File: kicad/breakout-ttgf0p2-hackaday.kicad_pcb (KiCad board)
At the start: 2 copper layers, 55 x 85 mm, 7 parts, among them J1 Conn_01x17, J2 Conn_01x20, J3 Conn_01x17, J4 Conn_01x20, U1 TT_GF_0p2_ASIC

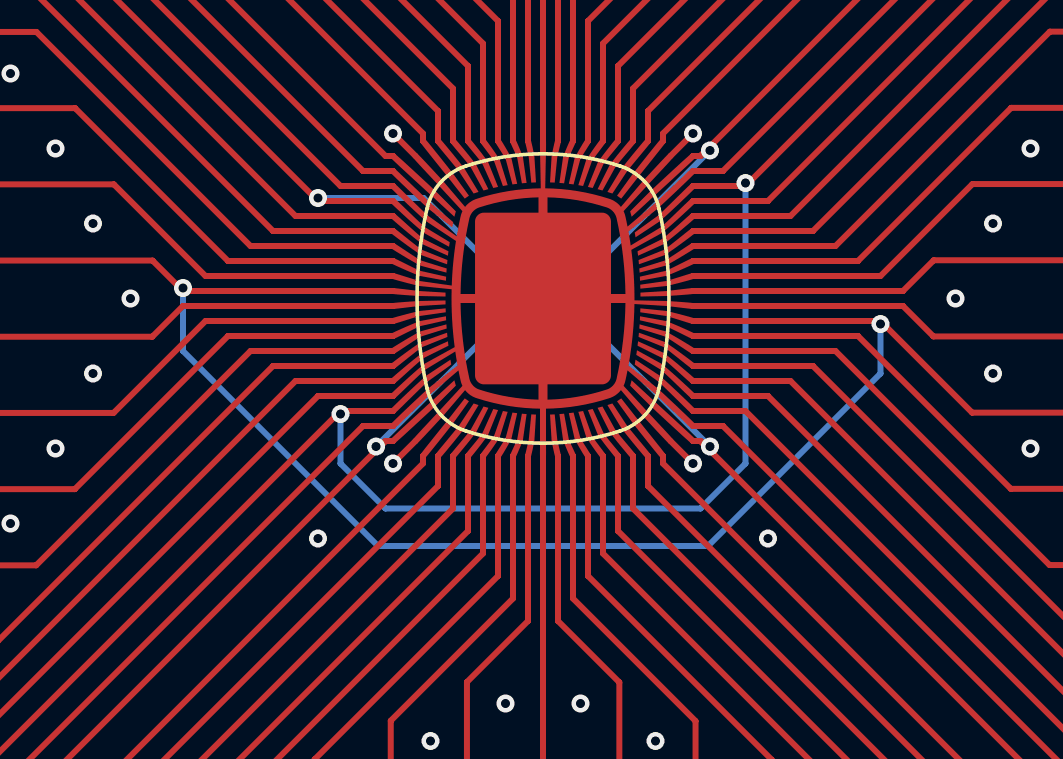
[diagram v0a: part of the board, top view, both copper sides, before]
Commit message: increase back-side spacing & remove fill
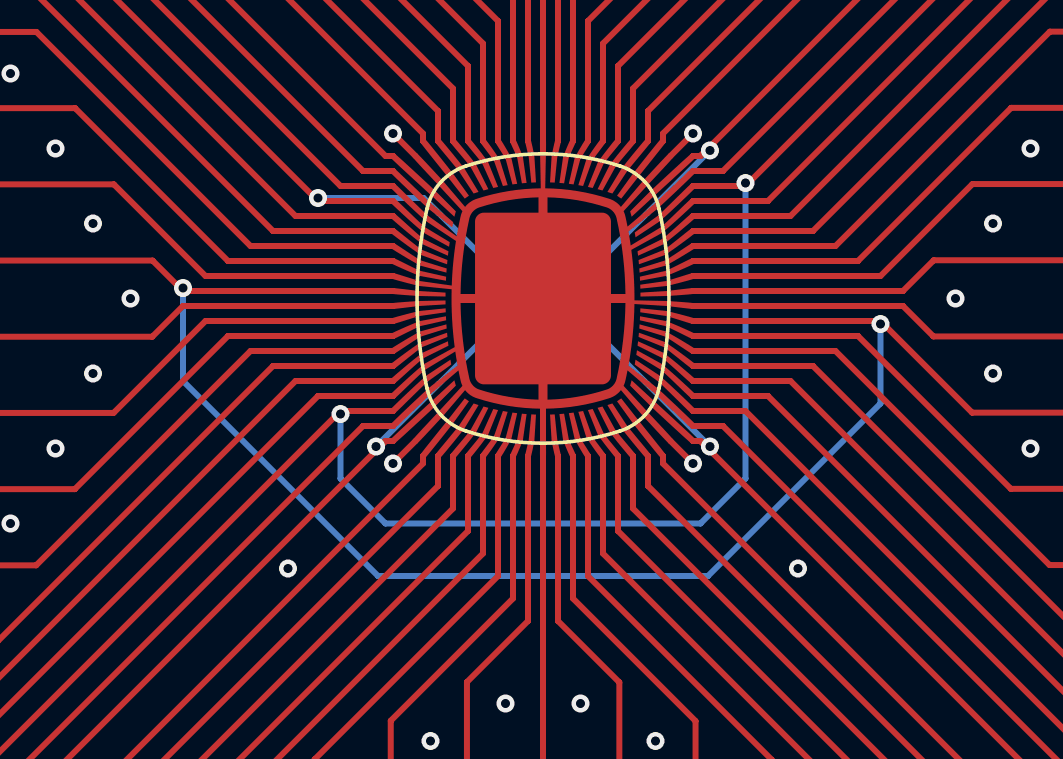
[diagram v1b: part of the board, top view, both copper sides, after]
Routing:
- net /VAA_Analog: track 75.7 -> 77.7 mm
- net /VDD_Core: track 80.4 -> 81.4 mm
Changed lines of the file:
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@@
 	)
 	(via
-		(at 130.25 108.75)
+		(at 129.25 109.75)
 		(size 0.6)
 		(drill 0.3)
@@
 	)
 	(via
-		(at 145.25 108.75)
+		(at 146.25 109.75)
 		(size 0.6)
 		(drill 0.3)
@@
 	)
 	(segment
-		(start 149 103.25)
-		(end 149 101.6)
+		(start 143.25 110)
+		(end 149 104.25)
 		(width 0.2)
 		(layer "B.Cu")
@@
 	)
 	(segment
-		(start 125.75 100.4)
-		(end 125.75 102.5)
+		(start 132.25 110)
+		(end 143.25 110)
 		(width 0.2)
 		(layer "B.Cu")
@@
 	)
 	(segment
-		(start 132.25 109)
-		(end 143.25 109)
+		(start 125.75 103.5)
+		(end 132.25 110)
 		(width 0.2)
 		(layer "B.Cu")
@@
 	)
 	(segment
-		(start 125.75 102.5)
-		(end 132.25 109)
+		(start 149 104.25)
+		(end 149 101.6)
 		(width 0.2)
 		(layer "B.Cu")
@@
 	)
 	(segment
-		(start 143.25 109)
-		(end 149 103.25)
+		(start 125.75 100.4)
+		(end 125.75 103.5)
 		(width 0.2)
 		(layer "B.Cu")
@@
 	)
 	(segment
-		(start 131 104.6)
-		(end 131 106.25)
+		(start 132.5 108.25)
+		(end 143 108.25)
 		(width 0.2)
 		(layer "B.Cu")
@@
 	)
 	(segment
-		(start 144.5 106.25)
-		(end 144.5 96.9)
+		(start 143 108.25)
+		(end 144.5 106.75)
 		(width 0.2)
 		(layer "B.Cu")
@@
 	)
 	(segment
-		(start 131 106.25)
-		(end 132.5 107.75)
+		(start 144.5 106.75)
+		(end 144.5 96.9)
 		(width 0.2)
 		(layer "B.Cu")
@@
 	)
 	(segment
-		(start 143 107.75)
-		(end 144.5 106.25)
+		(start 131 106.75)
+		(end 132.5 108.25)
 		(width 0.2)
 		(layer "B.Cu")
@@
 	)
 	(segment
-		(start 132.5 107.75)
-		(end 143 107.75)
+		(start 131 104.6)
+		(end 131 106.75)
 		(width 0.2)
 		(layer "B.Cu")
@@
 		(min_thickness 0.25)
 		(filled_areas_thickness no)
-		(fill yes
+		(fill
 			(thermal_gap 0.5)
 			(thermal_bridge_width 0.5)
